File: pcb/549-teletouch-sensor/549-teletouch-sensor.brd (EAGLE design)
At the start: 75.9 x 76.2 mm, 87 parts, among them J1 RASPBERRYPI-40-PIN-GPIO_PTH, J2 RASPBERRYPI-40-PIN-GPIO_PTH

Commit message: updated sensor pcb
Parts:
- removed H1, H2, H3, H4: STAND-OFF, SparkFun-Hardware:STAND-OFF
- removed J2: RASPBERRYPI-40-PIN-GPIO_PTH, SparkFun-Connectors:2X20_SHROUDED
- added IC1, IC2: MCP23017SP, adafruit:DIL28-3
- added SENSOR_ENDS1, SENSOR_ENDS2: CONN_20X2, SparkFun-Connectors:2X20
- moved J1 88.2 mm to (92.7, 55.9)
- moved C38 70.1 mm to (5.08, 12.7), turned to 0 degrees
- moved C37 63.8 mm to (11.4, 12.7), turned to 0 degrees
- moved R28 61.0 mm to (50.8, 76.2), turned to 0 degrees
- moved R29 60.8 mm to (44.5, 76.2), turned to 0 degrees
- moved C40 59.5 mm to (43.2, 7.62), turned to 0 degrees
- moved C36 58.5 mm to (17.8, 12.7), turned to 0 degrees
- moved C39 57.5 mm to (49.5, 7.62), turned to 0 degrees
- moved C35 54.6 mm to (24.1, 12.7), turned to 0 degrees
- moved C10 54.0 mm to (17.8, 17.8), turned to 0 degrees
- moved R30 53.5 mm to (38.1, 76.2), turned to 0 degrees
- moved C34 52.5 mm to (30.5, 12.7), turned to 0 degrees
- moved C33 52.2 mm to (36.8, 12.7), turned to 0 degrees
- moved R27 51.6 mm to (6.35, 81.3), turned to 0 degrees
- moved C11 51.2 mm to (11.4, 17.8), turned to 0 degrees
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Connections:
- removed net GP41: J1.37
- removed net GP42: J1.7
- removed net GP43: J1.11
- removed net GP44: J1.12
- removed net GP45: J1.15
- removed net GP46: J1.16
- removed net GP47: J1.18
- removed net GP48: J1.22
- removed net GP49: J1.13
- removed net N$11: R10.2
- removed net N$12: R1.2
- removed net N$13: R2.2
- removed net N$14: R3.2
- removed net N$15: R4.2
- removed net N$16: R5.2
- removed net N$17: R6.2
- removed net N$18: R7.2
- removed net N$19: R8.2
- removed net N$20: R9.2
- removed net N$31: R20.2
- removed net N$32: R11.2
- removed net N$33: R12.2
- removed net N$34: R13.2
- removed net N$35: R14.2
- removed net N$36: R15.2
- removed net N$37: R16.2
- removed net N$38: R17.2
- removed net N$39: R18.2
- removed net N$40: R19.2
- removed net N$51: R30.2
- removed net N$52: R21.2
- removed net N$53: R22.2
- removed net N$54: R23.2
- removed net N$55: R24.2
- removed net N$56: R25.2
- removed net N$57: R26.2
- removed net N$58: R27.2
- removed net N$59: R28.2
- removed net N$60: R29.2
- removed net N$71: R40.2
- removed net N$72: R31.2
- removed net N$73: R32.2
- removed net N$74: R33.2
- removed net N$75: R34.2
- removed net N$76: R35.2
- removed net N$77: R36.2
- removed net N$78: R37.2
- removed net N$79: R38.2
- removed net N$80: R39.2
- new net S1: R10.2, SENSOR_ENDS1.1
- new net S10: R9.2, SENSOR_ENDS1.19
- new net S11: R20.2, SENSOR_ENDS1.21
- new net S12: R11.2, SENSOR_ENDS1.23
- new net S13: R12.2, SENSOR_ENDS1.25
- new net S14: R13.2, SENSOR_ENDS1.27
- new net S15: R14.2, SENSOR_ENDS1.29
- new net S16: R15.2, SENSOR_ENDS1.31
- new net S17: R16.2, SENSOR_ENDS1.33
- new net S18: R17.2, SENSOR_ENDS1.35
- new net S19: R18.2, SENSOR_ENDS1.37
- new net S2: R1.2, SENSOR_ENDS1.3
- new net S20: R19.2, SENSOR_ENDS1.39
- new net S21: R30.2, SENSOR_ENDS1.2
- new net S22: R21.2, SENSOR_ENDS1.4
- new net S23: R22.2, SENSOR_ENDS1.6
- new net S24: R23.2, SENSOR_ENDS1.8
- new net S25: R24.2, SENSOR_ENDS1.10
- new net S26: R25.2, SENSOR_ENDS1.12
- new net S27: R26.2, SENSOR_ENDS1.14
- new net S28: R27.2, SENSOR_ENDS1.16
- new net S29: R28.2, SENSOR_ENDS1.18
- new net S3: R2.2, SENSOR_ENDS1.5
- new net S30: R29.2, SENSOR_ENDS1.20
- new net S31: R40.2, SENSOR_ENDS1.22
- new net S32: R31.2, SENSOR_ENDS1.24
- new net S33: R32.2, SENSOR_ENDS1.26
- new net S34: R33.2, SENSOR_ENDS1.28
- new net S35: R34.2, SENSOR_ENDS1.30
- new net S36: R35.2, SENSOR_ENDS1.32
- new net S37: R36.2, SENSOR_ENDS1.34
- new net S38: R37.2, SENSOR_ENDS1.36
- new net S39: R38.2, SENSOR_ENDS1.38
- new net S4: R3.2, SENSOR_ENDS1.7
- new net S40: R39.2, SENSOR_ENDS1.40
- new net S5: R4.2, SENSOR_ENDS1.9
- new net S6: R5.2, SENSOR_ENDS1.11
- new net S7: R6.2, SENSOR_ENDS1.13
- new net S8: R7.2, SENSOR_ENDS1.15
- new net S9: R8.2, SENSOR_ENDS1.17
- net GND: now also IC1.10, IC1.15, IC1.16, IC1.17, IC2.10, IC2.16, IC2.17
- net GP1: now also IC2.21, SENSOR_ENDS2.1; no longer J2.8
- net GP10: now also IC2.2, SENSOR_ENDS2.19; no longer J2.12
- net GP11: now also IC2.3, SENSOR_ENDS2.21; no longer J2.15
- net GP12: now also IC2.4, SENSOR_ENDS2.23; no longer J2.16
- net GP13: now also IC2.5, SENSOR_ENDS2.25; no longer J2.18
- net GP14: now also IC2.6, SENSOR_ENDS2.27; no longer J2.22
- net GP15: now also IC2.7, SENSOR_ENDS2.29; no longer J2.13
- net GP16: now also IC2.8, SENSOR_ENDS2.31; no longer J2.27
- net GP17: now also IC1.21, SENSOR_ENDS2.33; no longer J2.28
- net GP18: now also IC1.22, SENSOR_ENDS2.35; no longer J2.2
- net GP19: now also IC1.23, SENSOR_ENDS2.37; no longer J2.4
- net GP2: now also IC2.22, SENSOR_ENDS2.3; no longer J2.10
- net GP20: now also IC1.24, SENSOR_ENDS2.39; no longer J2.1
- net GP21: now also IC1.25, SENSOR_ENDS2.2; no longer J2.17
- net GP22: now also IC1.26, SENSOR_ENDS2.4; no longer J2.29
- net GP23: now also IC1.27, SENSOR_ENDS2.6; no longer J2.31
- net GP24: now also IC1.28, SENSOR_ENDS2.8; no longer J2.32
- net GP25: now also IC1.1, SENSOR_ENDS2.10; no longer J2.33
- net GP26: now also IC1.2, SENSOR_ENDS2.12; no longer J2.36
- net GP27: now also IC1.3, SENSOR_ENDS2.14; no longer J2.35
- net GP28: now also IC1.4, SENSOR_ENDS2.16; no longer J2.38
- net GP29: now also IC1.5, SENSOR_ENDS2.18; no longer J2.40
- net GP3: now also IC2.23, SENSOR_ENDS2.5; no longer J2.23
- net GP30: now also IC1.6, SENSOR_ENDS2.20; no longer J2.37
- net GP31: now also IC1.7, SENSOR_ENDS2.22; no longer J2.6
- net GP32: now also IC1.8, SENSOR_ENDS2.24; no longer J2.9
- net GP33: now also SENSOR_ENDS2.26; no longer J2.14
- net GP34: now also SENSOR_ENDS2.28; no longer J2.20
- net GP35: now also SENSOR_ENDS2.30; no longer J2.25
- net GP36: now also SENSOR_ENDS2.32; no longer J2.30
- net GP37: now also SENSOR_ENDS2.34; no longer J2.34
- net GP38: now also SENSOR_ENDS2.36; no longer J2.39
- net GP39: now also SENSOR_ENDS2.38; no longer J2.3
- net GP4: now also IC2.24, SENSOR_ENDS2.7; no longer J2.21
- net GP40: now also SENSOR_ENDS2.40; no longer J2.5
- net GP5: now also IC2.25, SENSOR_ENDS2.9; no longer J2.19
- net GP6: now also IC2.26, SENSOR_ENDS2.11; no longer J2.24
- net GP7: now also IC2.27, SENSOR_ENDS2.13; no longer J2.26
- net GP8: now also IC2.28, SENSOR_ENDS2.15; no longer J2.7
- net GP9: now also IC2.1, SENSOR_ENDS2.17; no longer J2.11
- net SCL: now also IC1.12, IC2.12
- net SDA: now also IC1.13, IC2.13
- net VDD: now also IC1.18, IC1.9, IC2.15, IC2.18, IC2.9
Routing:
- net GP28: track 43.3 -> 169.6 mm
- net GP31: track 26.8 -> 144.7 mm, vias 1 -> 2
- net SCL: track 0.00 -> 115.4 mm
- net GP26: track 37.5 -> 145.0 mm, vias 1 -> 3
- net GP27: track 38.7 -> 144.7 mm, vias 1 -> 2
- net VDD: track 0.00 -> 105.5 mm
- net SDA: track 0.00 -> 100.8 mm
- net GP17: track 34.3 -> 133.6 mm, vias 1 -> 5
- net GP22: track 28.8 -> 125.9 mm, vias 1 -> 3
- net GP23: track 33.2 -> 117.3 mm, vias 0 -> 4
- net S23: track 0.00 -> 82.0 mm
- net GP4: track 38.7 -> 117.0 mm, vias 1 -> 2
- net GP25: track 31.4 -> 109.3 mm, vias 1 -> 3
- net S22: track 0.00 -> 76.3 mm, vias 0 -> 2
- net GP1: track 21.3 -> 93.4 mm, vias 0 -> 1
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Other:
- board size 75.9 x 76.2 mm -> 101.3 x 86.3 mm
- board text removed: "team12"

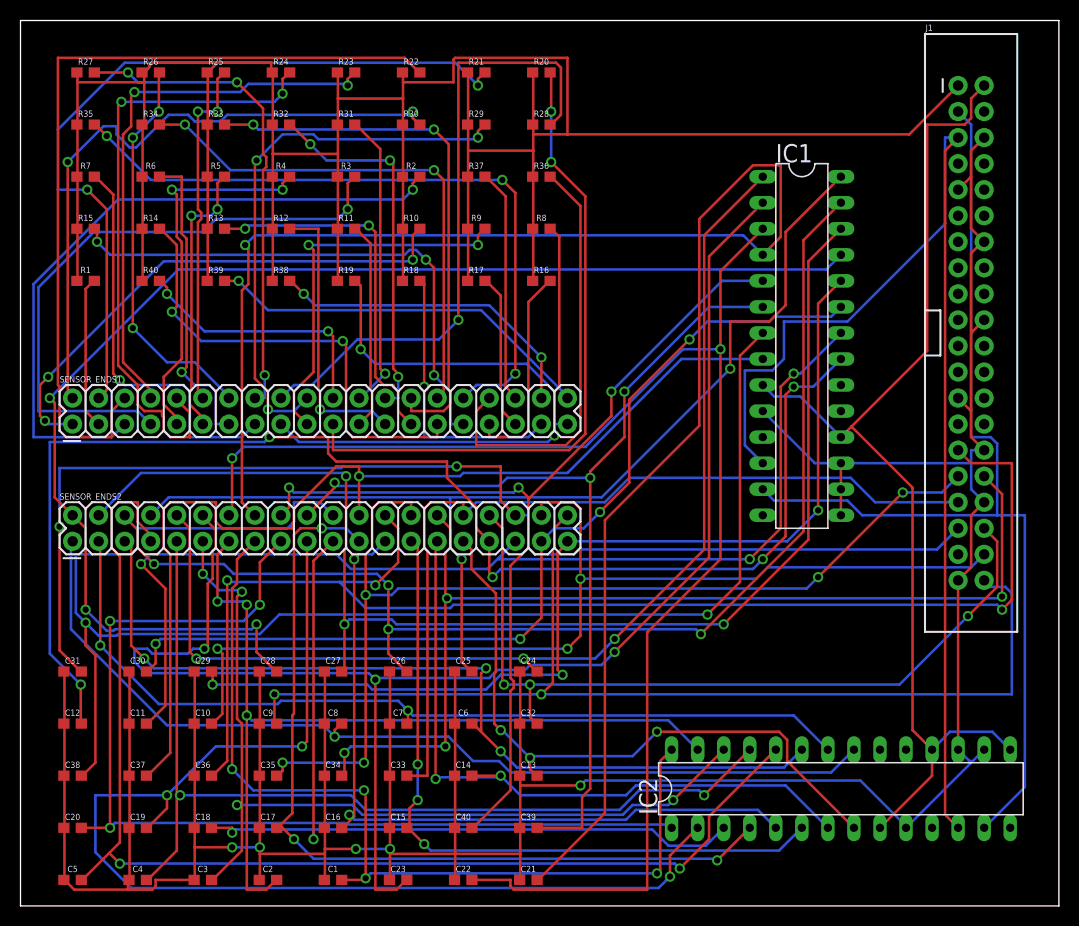
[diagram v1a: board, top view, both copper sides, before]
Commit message: updated to half the amount of sensors
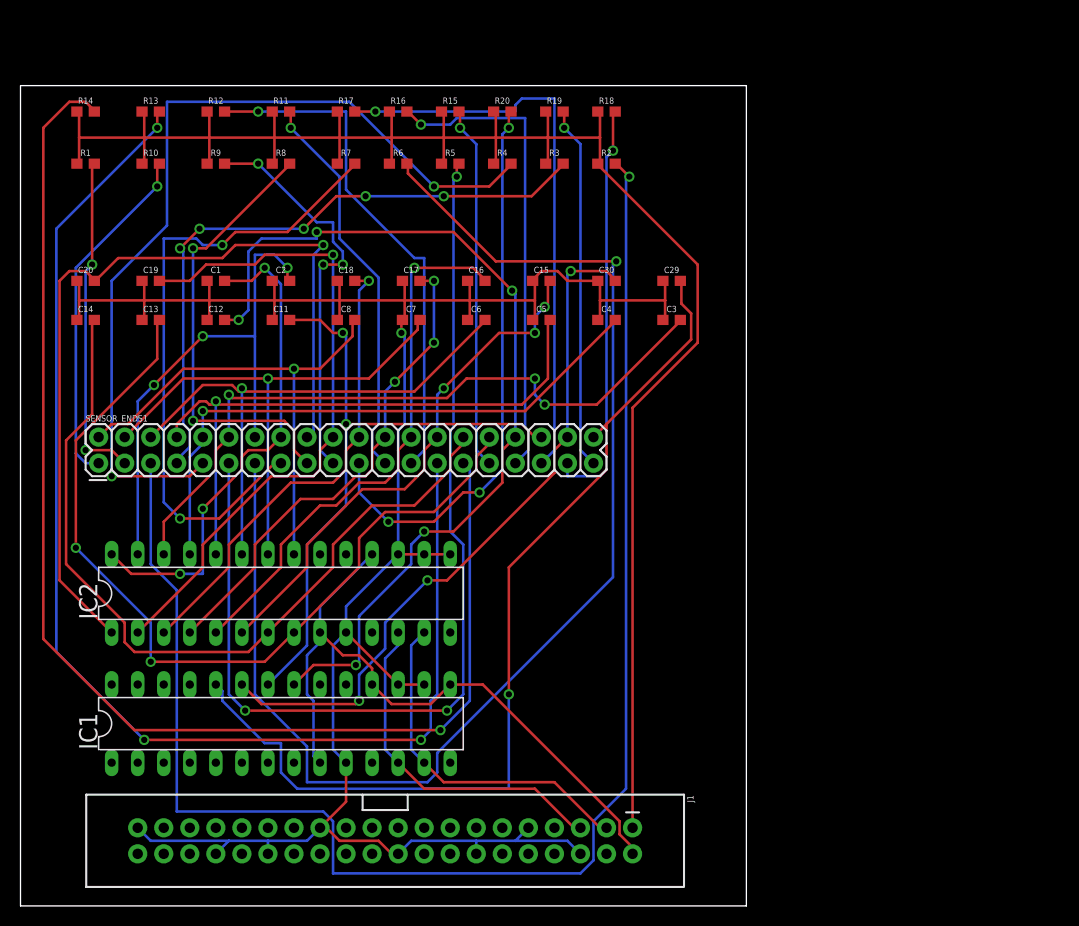
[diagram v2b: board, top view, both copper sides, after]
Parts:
- removed C10, C21, C22, C23, C24, C25, C26, C27, C28, C31, C32, C33, C34, C35, C36, C37, C38, C39, C40, C9: 47nF, SparkFun-Capacitors:0603
- removed R21, R22, R23, R24, R25, R26, R27, R28, R29, R30, R31, R32, R33, R34, R35, R36, R37, R38, R39, R40: 2.2k, SparkFun-Resistors:0603
- removed SENSOR_ENDS2: CONN_20X2, SparkFun-Connectors:2X20
- moved J1 75.6 mm to (35.6, 6.35), turned to 270 degrees
- moved C3 71.2 mm to (63.5, 57.1)
- moved C4 71.2 mm to (57.1, 57.1)
- moved C5 71.2 mm to (50.8, 57.1)
- moved IC1 62.7 mm to (25.4, 17.8), turned to 0 degrees
- moved C1 59.5 mm to (19.1, 61.0)
- moved C29 59.5 mm to (63.5, 61.0)
- moved C30 59.5 mm to (57.1, 61.0)
- moved C2 58.4 mm to (25.4, 61.0)
- moved IC2 57.8 mm to (25.4, 30.5)
- moved C13 57.7 mm to (12.7, 57.1)
- moved C14 57.7 mm to (6.35, 57.1)
- moved C15 55.1 mm to (50.8, 61.0)
- moved C16 55.1 mm to (44.5, 61.0)
- moved C17 55.1 mm to (38.1, 61.0)
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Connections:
- removed net GP21: C28.2, IC1.25, SENSOR_ENDS2.2
- removed net GP22: C27.2, IC1.26, SENSOR_ENDS2.4
- removed net GP23: C26.2, IC1.27, SENSOR_ENDS2.6
- removed net GP24: C25.2, IC1.28, SENSOR_ENDS2.8
- removed net GP25: C24.2, IC1.1, SENSOR_ENDS2.10
- removed net GP26: C23.2, IC1.2, SENSOR_ENDS2.12
- removed net GP27: C22.2, IC1.3, SENSOR_ENDS2.14
- removed net GP28: C21.2, IC1.4, SENSOR_ENDS2.16
- removed net GP29: C40.2, IC1.5, SENSOR_ENDS2.18
- removed net GP30: C39.2, IC1.6, SENSOR_ENDS2.20
- removed net GP31: C38.2, IC1.7, SENSOR_ENDS2.22
- removed net GP32: C37.2, IC1.8, SENSOR_ENDS2.24
- removed net GP33: C36.2, J1.29, SENSOR_ENDS2.26
- removed net GP34: C35.2, J1.31, SENSOR_ENDS2.28
- removed net GP35: C34.2, J1.32, SENSOR_ENDS2.30
- removed net GP36: C33.2, J1.33, SENSOR_ENDS2.32
- removed net GP37: C32.2, J1.36, SENSOR_ENDS2.34
- removed net GP38: C31.2, J1.35, SENSOR_ENDS2.36
- removed net GP39: C10.2, J1.38, SENSOR_ENDS2.38
- removed net GP40: C9.2, J1.40, SENSOR_ENDS2.40
- removed net S21: R30.2, SENSOR_ENDS1.2
- removed net S22: R21.2, SENSOR_ENDS1.4
- removed net S23: R22.2, SENSOR_ENDS1.6
- removed net S24: R23.2, SENSOR_ENDS1.8
- removed net S25: R24.2, SENSOR_ENDS1.10
- removed net S26: R25.2, SENSOR_ENDS1.12
- removed net S27: R26.2, SENSOR_ENDS1.14
- removed net S28: R27.2, SENSOR_ENDS1.16
- removed net S29: R28.2, SENSOR_ENDS1.18
- removed net S30: R29.2, SENSOR_ENDS1.20
- removed net S31: R40.2, SENSOR_ENDS1.22
- removed net S32: R31.2, SENSOR_ENDS1.24
- removed net S33: R32.2, SENSOR_ENDS1.26
- removed net S34: R33.2, SENSOR_ENDS1.28
- removed net S35: R34.2, SENSOR_ENDS1.30
- removed net S36: R35.2, SENSOR_ENDS1.32
- removed net S37: R36.2, SENSOR_ENDS1.34
- removed net S38: R37.2, SENSOR_ENDS1.36
- removed net S39: R38.2, SENSOR_ENDS1.38
- removed net S40: R39.2, SENSOR_ENDS1.40
- net GND: now also IC2.15; no longer C10.1, C21.1, C22.1, C23.1, C24.1, C25.1, C26.1, C27.1, C28.1, C31.1, C32.1, C33.1, C34.1, C35.1, C36.1, C37.1, C38.1, C39.1, C40.1, C9.1, IC1.15
- net GP1: now also SENSOR_ENDS1.2; no longer SENSOR_ENDS2.1
- net GP10: now also SENSOR_ENDS1.20; no longer SENSOR_ENDS2.19
- net GP11: now also SENSOR_ENDS1.22; no longer SENSOR_ENDS2.21
- net GP12: now also SENSOR_ENDS1.24; no longer SENSOR_ENDS2.23
- net GP13: now also SENSOR_ENDS1.26; no longer SENSOR_ENDS2.25
- net GP14: now also SENSOR_ENDS1.28; no longer SENSOR_ENDS2.27
- net GP15: now also SENSOR_ENDS1.30; no longer SENSOR_ENDS2.29
- net GP16: now also SENSOR_ENDS1.32; no longer SENSOR_ENDS2.31
- net GP17: now also SENSOR_ENDS1.34; no longer SENSOR_ENDS2.33
- net GP18: now also SENSOR_ENDS1.36; no longer SENSOR_ENDS2.35
- net GP19: now also SENSOR_ENDS1.38; no longer SENSOR_ENDS2.37
- net GP2: now also SENSOR_ENDS1.4; no longer SENSOR_ENDS2.3
- net GP20: now also SENSOR_ENDS1.40; no longer SENSOR_ENDS2.39
- net GP3: now also SENSOR_ENDS1.6; no longer SENSOR_ENDS2.5
- net GP4: now also SENSOR_ENDS1.8; no longer SENSOR_ENDS2.7
- net GP5: now also SENSOR_ENDS1.10; no longer SENSOR_ENDS2.9
- net GP6: now also SENSOR_ENDS1.12; no longer SENSOR_ENDS2.11
- net GP7: now also SENSOR_ENDS1.14; no longer SENSOR_ENDS2.13
- net GP8: now also SENSOR_ENDS1.16; no longer SENSOR_ENDS2.15
- net GP9: now also SENSOR_ENDS1.18; no longer SENSOR_ENDS2.17
- net VCC: no longer R21.1, R22.1, R23.1, R24.1, R25.1, R26.1, R27.1, R28.1, R29.1, R30.1, R31.1, R32.1, R33.1, R34.1, R35.1, R36.1, R37.1, R38.1, R39.1, R40.1
- net VDD: now also IC1.15; no longer IC2.15
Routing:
- net GP28: track 169.6 -> 0.00 mm, vias 1 -> 0
- net GP26: track 145.0 -> 0.00 mm, vias 3 -> 0
- net GP27: track 144.7 -> 0.00 mm, vias 2 -> 0
- net GP31: track 144.7 -> 0.00 mm, vias 2 -> 0
- net GND: track 361.3 -> 221.9 mm, vias 5 -> 1
- net GP33: track 129.1 -> 0.00 mm, vias 3 -> 0
- net GP21: track 128.3 -> 0.00 mm, vias 3 -> 0
- net GP22: track 125.9 -> 0.00 mm, vias 3 -> 0
- net GP23: track 117.3 -> 0.00 mm, vias 4 -> 0
- net GP38: track 116.9 -> 0.00 mm, vias 2 -> 0
- net GP25: track 109.3 -> 0.00 mm, vias 3 -> 0
- net GP40: track 106.5 -> 0.00 mm, vias 2 -> 0
- net GP24: track 105.8 -> 0.00 mm, vias 2 -> 0
- net GP35: track 102.6 -> 0.00 mm, vias 4 -> 0
- net GP34: track 102.5 -> 0.00 mm, vias 5 -> 0
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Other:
- board size 101.3 x 86.3 mm -> 70.8 x 80 mm

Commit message: add name and clean up
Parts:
- moved C29 8.03 mm to (55.9, 58.4)
- moved C3 8.03 mm to (55.9, 54.6)
- moved C30 6.84 mm to (50.8, 58.4)
- moved C4 6.84 mm to (50.8, 54.6)
- moved C15 5.68 mm to (45.7, 58.4)
- moved C5 5.68 mm to (45.7, 54.6)
- moved R19 5.24 mm to (50.8, 72.4)
- moved R20 5.24 mm to (45.7, 72.4)
- moved R3 5.24 mm to (50.8, 67.3)
- moved R4 5.24 mm to (45.7, 67.3)
- moved R10 5.24 mm to (11.4, 67.3)
- moved R11 5.24 mm to (24.1, 72.4)
- moved R12 5.24 mm to (17.8, 72.4)
- moved R13 5.24 mm to (11.4, 72.4)
- moved R17 5.24 mm to (30.5, 72.4)
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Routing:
- net S3: track 151.7 -> 63.3 mm, vias 1 -> 5
- net S7: track 128.3 -> 40.9 mm, vias 1 -> 5
- net S12: track 38.7 -> 96.1 mm, vias 1 -> 4
- net GP8: track 48.9 -> 100.6 mm
- net S13: track 50.4 -> 101.0 mm, vias 1 -> 4
- net S16: track 35.6 -> 79.9 mm, vias 1 -> 2
- net S15: track 126.4 -> 89.7 mm, vias 1 -> 2
- net S8: track 62.4 -> 32.8 mm, vias 2 -> 3
- net GP14: track 51.3 -> 78.2 mm, vias 3 -> 2
- net GP19: track 68.8 -> 95.1 mm, vias 3 -> 2
- net S14: track 123.8 -> 104.4 mm, vias 3 -> 2
- net GP18: track 62.9 -> 81.3 mm, vias 2 -> 3
- net GND: track 221.9 -> 239.7 mm
- net S9: track 43.8 -> 26.2 mm, vias 2 -> 3
- net S5: track 86.2 -> 103.8 mm
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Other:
- board size 70.8 x 80 mm -> 67 x 76.2 mm
- board text added: "team12"
